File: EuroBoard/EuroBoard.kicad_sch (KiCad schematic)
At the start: 13 parts, among them J1 UART, SW1 SW_SPST, U2 STM32G030CxT, Y1 16MHz

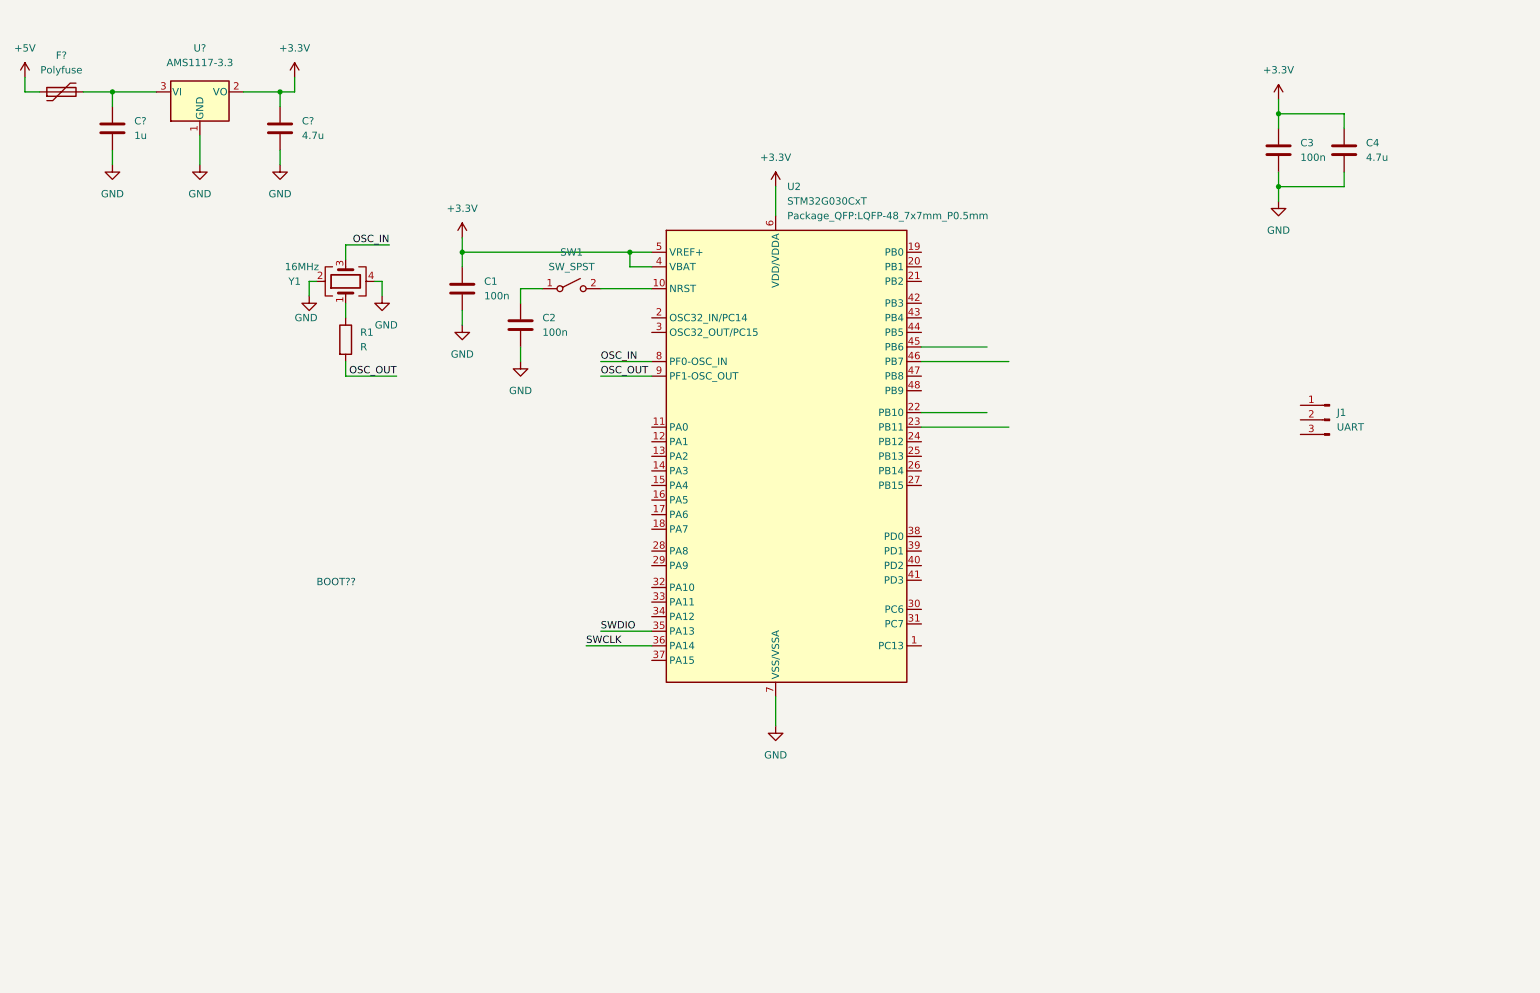
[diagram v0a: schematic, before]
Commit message: EuroBoard connector added
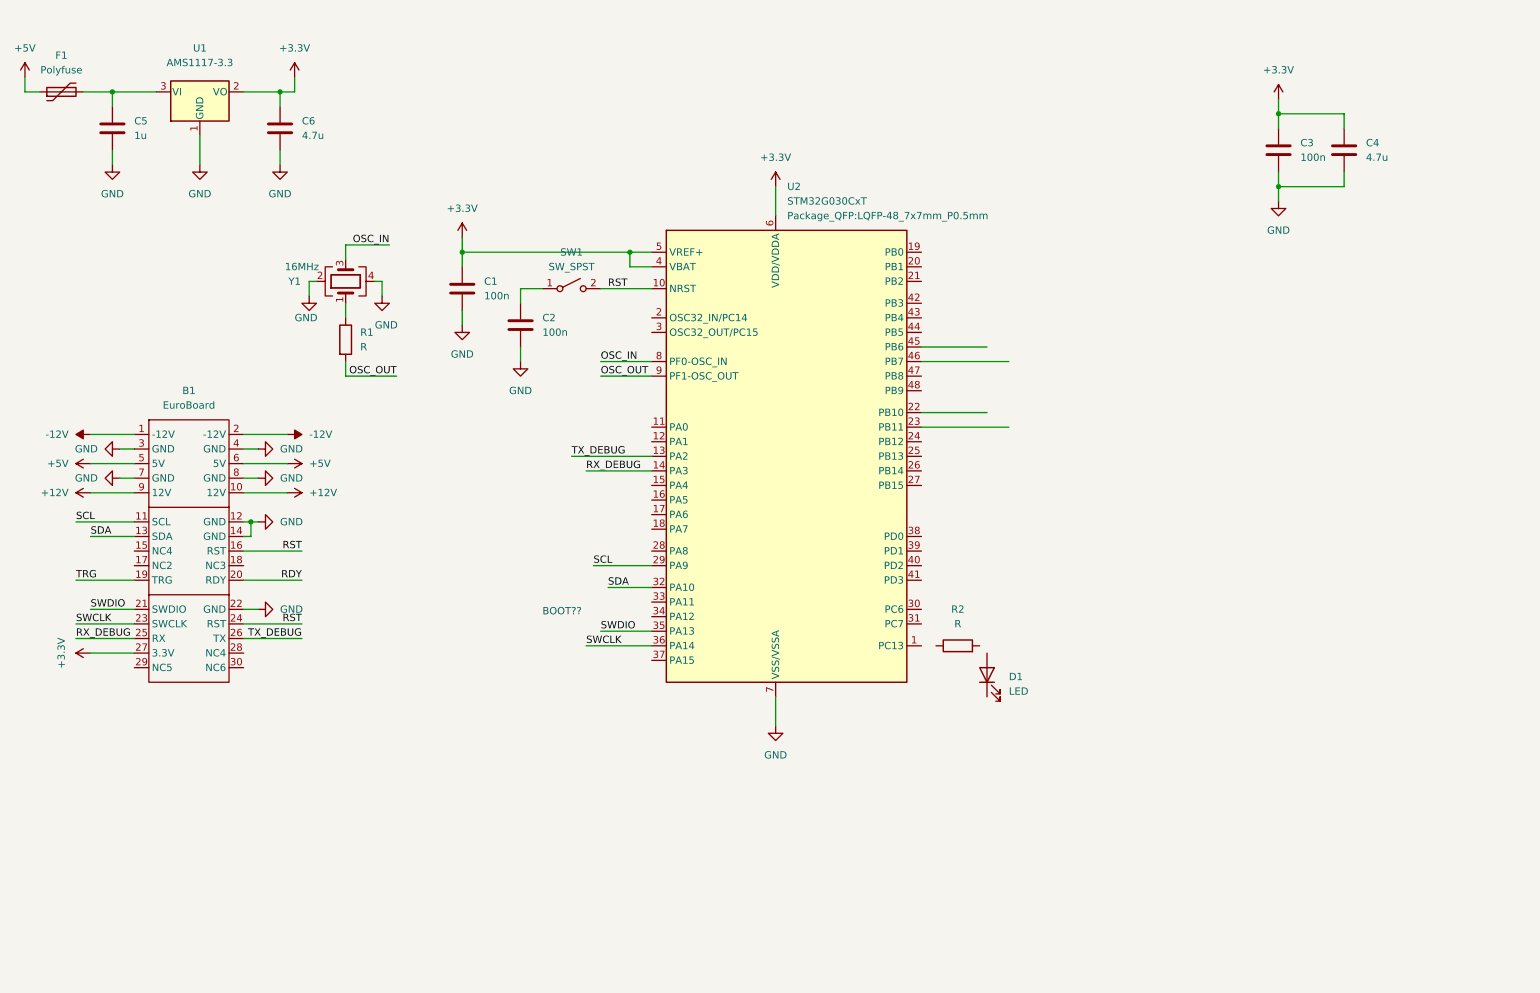
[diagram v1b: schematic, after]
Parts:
- removed J1: UART, symbol Connector:Conn_01x03_Male
- added B1: EuroBoard, MEMS_Custom:EuroMeasure, symbol MEMS_Custom:EuroBoard
- added D1: LED, symbol Device:LED
- added R2: R, Resistor_SMD:R_0805_2012Metric_Pad1.20x1.40mm_HandSolder, symbol Device:R
- C1, C2, C3, C4: footprint (none) -> Capacitor_SMD:C_0805_2012Metric_Pad1.18x1.45mm_HandSolder
- C5, C6: renamed from C?; footprint (none) -> Capacitor_SMD:C_0805_2012Metric_Pad1.18x1.45mm_HandSolder
- R1: footprint (none) -> Resistor_SMD:R_0805_2012Metric_Pad1.20x1.40mm_HandSolder
- Y1: footprint (none) -> Oscillator:Oscillator_SMD_Abracon_ASDMB-4Pin_2.5x2.0mm
- gave numbers to parts that had none: 2
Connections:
- net +3.3V: now also B1.27 (3.3V)
- net +5V: now also B1.5 (5V), B1.6 (5V)
- net GND: now also B1.12 (GND), B1.14 (GND), B1.22 (GND), B1.3 (GND), B1.4 (GND), B1.7 (GND), B1.8 (GND)
- net SWCLK: now also B1.23 (SWCLK)
- net SWDIO: now also B1.21 (SWDIO)
- net RST: now reaches SW1.2 (B), U2.10 (NRST)
- net RST: now also B1.16 (RST), B1.24 (RST)
- net TX_DEBUG: now reaches U2.13 (PA2)
- net TX_DEBUG: now also B1.26 (TX)
- net RX_DEBUG: now reaches U2.14 (PA3)
- net RX_DEBUG: now also B1.25 (RX)
- net SCL: now reaches U2.29 (PA9)
- net SCL: now also B1.11 (SCL)
- net SDA: now reaches U2.32 (PA10)
- net SDA: now also B1.13 (SDA)
- new net +12V: B1.10 (12V), B1.9 (12V)
- new net -12V: B1.1 (-12V), B1.2 (-12V)
- new net RDY: B1.20 (RDY)
- new net TRG: B1.19 (TRG)

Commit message: mend
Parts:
- added R?: R, Resistor_SMD:R_0805_2012Metric_Pad1.20x1.40mm_HandSolder, symbol Device:R
- added SW?: BOOT, Button_Switch_SMD:SW_SPST_B3U-1000P-B, symbol Switch:SW_SPST
- SW1: value SW_SPST -> RESET
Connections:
- net +3.3V: now also SW?.1 (A)
- net GND: now also D1.1 (K)
- net SWCLK: now also R?.1
- net at R2.1: now also D1.2 (A)
- net at R2.2: now also U2.1 (PC13)
- new net: R?.2, SW?.2 (B)
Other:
- moved on the sheet: D1, R2

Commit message: Almost done
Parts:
- removed R?: R, Resistor_SMD:R_0805_2012Metric_Pad1.20x1.40mm_HandSolder, symbol Device:R
- removed SW?: BOOT, Button_Switch_SMD:SW_SPST_B3U-1000P-B, symbol Switch:SW_SPST
- added C7: C, Capacitor_SMD:C_0805_2012Metric_Pad1.18x1.45mm_HandSolder, symbol Device:C
- added C8: 100n, Capacitor_SMD:C_0805_2012Metric_Pad1.18x1.45mm_HandSolder, symbol Device:C
- added D?: 1n4148, Diode_SMD:D_SOD-123, symbol Device:D
- added J1: SPI, Connector_PinHeader_2.54mm:PinHeader_1x04_P2.54mm_Vertical, symbol Connector:Conn_01x04_Male
- added J?: UART, symbol Connector:Conn_01x03_Male
- added J?: I2C, symbol Connector:Conn_01x03_Male
- added L1: L_Ferrite, Inductor_SMD:L_0805_2012Metric, symbol Device:L_Ferrite
- C1: value 100n -> C
- D1: footprint (none) -> LED_SMD:LED_0805_2012Metric_Pad1.15x1.40mm_HandSolder
- F1: footprint (none) -> Fuse:Fuse_1210_3225Metric
- R2: value R -> 1k
- SW1: footprint Button_Switch_SMD:SW_SPST_B3U-1000P-B -> Button_Switch_SMD:SW_SPST_B3S-1000
- Y1: value 16MHz -> NX2520 16MHz
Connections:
- net +3.3V: no longer C1.1, U2.5 (VREF+)
- net GND: now also SW1.1 (A), C7.2, C8.2, J1.4 (Pin_4), J?.3 (Pin_3), J?.3 (Pin_3)
- net OSC_IN: now also C1.1
- net RST: now also D?.1 (K); no longer SW1.2 (B), U2.10 (NRST)
- net SCL: now also U2.45 (PB6); no longer U2.29 (PA9)
- net SDA: now also U2.46 (PB7); no longer U2.32 (PA10)
- net at C5.1, U1.3 (VI): now also L1.2; no longer F1.2
- net at C2.1: now also SW1.2 (B), U2.10 (NRST), D?.2 (A); no longer SW1.1 (A)
- net LED: now reaches R2.2, U2.1 (PC13)
- net SPI1_SCK: now reaches U2.12 (PA1)
- net SPI1_SCK: now also J1.1 (Pin_1)
- net SPI1_MISO: now reaches U2.17 (PA6)
- net SPI1_MISO: now also J1.2 (Pin_2), J1.3 (Pin_3)
- net SPI1_MOSI: now reaches U2.18 (PA7)
- net SCL2: now reaches U2.22 (PB10)
- net SCL2: now also J?.1 (Pin_1)
- net SDA2: now reaches U2.23 (PB11)
- net SDA2: now also J?.2 (Pin_2)
- net at R1.1, Y1.1: now also C7.1
- new net: F1.2, L1.1
- new net RX_AUX: J?.2 (Pin_2), U2.32 (PA10)
- new net TX_AUX: J?.1 (Pin_1), U2.29 (PA9)
- new net VREF: C8.1, U2.5 (VREF+)
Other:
- note added: "BOOT0"
- note removed: "BOOT??"
- moved on the sheet: B1, C2, C3, C4, C5, C6, D1, F1, R1, R2, SW1, U1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

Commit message: Almost done
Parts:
- gave numbers to parts that had none: 3
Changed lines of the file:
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@@
   (symbol (lib_id "Connector:Conn_01x03_Male") (at 241.3 109.22 0) (unit 1)
     (in_bom yes) (on_board yes) (fields_autoplaced)
-    (property "Reference" "J?" (id 0) (at 241.935 101.6 0))
+    (property "Reference" "J3" (id 0) (at 241.935 101.6 0))
     (property "Value" "UART" (id 1) (at 241.935 104.14 0))
     (property "Footprint" "" (id 2) (at 241.3 109.22 0)
@@
   (symbol (lib_id "power:GND") (at 248.92 111.76 0) (unit 1)
     (in_bom yes) (on_board yes) (fields_autoplaced)
-    (property "Reference" "#PWR?" (id 0) (at 248.92 118.11 0)
+    (property "Reference" "#PWR0105" (id 0) (at 248.92 118.11 0)
       (effects (font (size 1.27 1.27)) hide)
     )
@@
   (symbol (lib_id "Connector:Conn_01x03_Male") (at 241.3 91.44 0) (unit 1)
     (in_bom yes) (on_board yes) (fields_autoplaced)
-    (property "Reference" "J?" (id 0) (at 241.935 83.82 0))
+    (property "Reference" "J2" (id 0) (at 241.935 83.82 0))
     (property "Value" "I2C" (id 1) (at 241.935 86.36 0))
     (property "Footprint" "" (id 2) (at 241.3 91.44 0)
@@
   (symbol (lib_id "Device:D") (at 97.79 64.77 0) (unit 1)
     (in_bom yes) (on_board yes) (fields_autoplaced)
-    (property "Reference" "D?" (id 0) (at 97.79 58.42 0))
+    (property "Reference" "D2" (id 0) (at 97.79 58.42 0))
     (property "Value" "1n4148" (id 1) (at 97.79 60.96 0))
     (property "Footprint" "Diode_SMD:D_SOD-123" (id 2) (at 97.79 64.77 0)
@@
   (symbol (lib_id "power:GND") (at 248.92 93.98 0) (unit 1)
     (in_bom yes) (on_board yes) (fields_autoplaced)
-    (property "Reference" "#PWR?" (id 0) (at 248.92 100.33 0)
+    (property "Reference" "#PWR0128" (id 0) (at 248.92 100.33 0)
       (effects (font (size 1.27 1.27)) hide)
     )
@@
   (symbol (lib_id "power:GND") (at 250.19 41.91 0) (unit 1)
     (in_bom yes) (on_board yes) (fields_autoplaced)
-    (property "Reference" "#PWR?" (id 0) (at 250.19 48.26 0)
+    (property "Reference" "#PWR0129" (id 0) (at 250.19 48.26 0)
       (effects (font (size 1.27 1.27)) hide)
     )
@@
       (reference "#PWR0104") (unit 1) (value "GND") (footprint "")
     )
+    (path "/7d243bd9-5a2e-4326-8d2b-a5f1dfd1f8f3"
+      (reference "#PWR0105") (unit 1) (value "GND") (footprint "")
+    )
     (path "/302a3ca2-8721-479b-b4eb-f005cb527499"
       (reference "#PWR0106") (unit 1) (value "GND") (footprint "")
@@
       (reference "#PWR0127") (unit 1) (value "GND") (footprint "")
     )
-    (path "/7d243bd9-5a2e-4326-8d2b-a5f1dfd1f8f3"
-      (reference "#PWR?") (unit 1) (value "GND") (footprint "")
-    )
     (path "/c7143079-c7d7-419c-9261-2f446fb4d84f"
-      (reference "#PWR?") (unit 1) (value "GND") (footprint "")
+      (reference "#PWR0128") (unit 1) (value "GND") (footprint "")
     )
     (path "/e1d04403-db45-42b9-aeee-a12acba02ccf"
-      (reference "#PWR?") (unit 1) (value "GND") (footprint "")
+      (reference "#PWR0129") (unit 1) (value "GND") (footprint "")
     )
     (path "/d92283e0-1a84-4854-b416-29c1c54c41f7"
@@
     )
     (path "/acef170c-9dde-4b25-b979-ff4ef70a5cbb"
-      (reference "D?") (unit 1) (value "1n4148") (footprint "Diode_SMD:D_SOD-123")
+      (reference "D2") (unit 1) (value "1n4148") (footprint "Diode_SMD:D_SOD-123")
     )
     (path "/55ad175e-3839-4c69-a4d0-462ebdbf17e1"
@@
       (reference "J1") (unit 1) (value "SPI") (footprint "Connector_PinHeader_2.54mm:PinHeader_1x04_P2.54mm_Vertical")
     )
+    (path "/a131e4fd-2b6b-4ceb-827a-fe46605e4cbb"
+      (reference "J2") (unit 1) (value "I2C") (footprint "")
+    )
     (path "/2486761d-6715-4e29-a9bb-d5aae2207d95"
-      (reference "J?") (unit 1) (value "UART") (footprint "")
-    )
-    (path "/a131e4fd-2b6b-4ceb-827a-fe46605e4cbb"
-      (reference "J?") (unit 1) (value "I2C") (footprint "")
+      (reference "J3") (unit 1) (value "UART") (footprint "")
     )
     (path "/c2e8100f-910e-434c-951c-160188608971"

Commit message: Started doing PCB
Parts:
- added C10: 100n, Capacitor_SMD:C_0805_2012Metric_Pad1.18x1.45mm_HandSolder, symbol Device:C
- added C11, C9: 10u, Capacitor_SMD:C_0805_2012Metric_Pad1.18x1.45mm_HandSolder, symbol Device:C
- C4: value 4.7u -> 10u
- J2, J3: footprint (none) -> Connector_PinSocket_2.54mm:PinSocket_1x03_P2.54mm_Vertical
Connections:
- net +3.3V: now also L1.2, C10.1, C11.1; no longer C6.1, U1.2 (VO)
- net GND: now also C10.2, C11.2, C9.2
- net at C5.1, U1.3 (VI): now also F1.2, C9.1; no longer L1.2
- net at L1.1: now also C6.1, U1.2 (VO); no longer F1.2
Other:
- moved on the sheet: C5, C6, F1, L1, U1

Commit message: Board outline
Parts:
- removed J1: SPI, Connector_PinHeader_2.54mm:PinHeader_1x04_P2.54mm_Vertical, symbol Connector:Conn_01x04_Male
- removed J2: I2C, Connector_PinSocket_2.54mm:PinSocket_1x03_P2.54mm_Vertical, symbol Connector:Conn_01x03_Male
- added C12, C13, C14, C15: 10u, Capacitor_SMD:C_0805_2012Metric_Pad1.18x1.45mm_HandSolder, symbol Device:C
- added J1: GPIO, Connector_PinHeader_2.54mm:PinHeader_1x08_P2.54mm_Vertical, symbol Connector:Conn_01x08_Male
- added J2: Conn_01x07_Male, Connector_PinHeader_2.54mm:PinHeader_1x07_P2.54mm_Vertical, symbol Connector:Conn_01x07_Male
- added J4: Conn_01x05_Male, Connector_PinHeader_2.54mm:PinHeader_1x05_P2.54mm_Vertical, symbol Connector:Conn_01x05_Male
- added SW2: SW_DIP_x04, Button_Switch_SMD:SW_DIP_SPSTx04_Slide_Omron_A6H-4101_W6.15mm_P1.27mm, symbol Switch:SW_DIP_x04
- C4: value 10u -> 4.7u
- J3: value UART -> I2C; footprint Connector_PinSocket_2.54mm:PinSocket_1x03_P2.54mm_Vertical -> Connector_PinHeader_2.54mm:PinHeader_1x03_P2.54mm_Vertical
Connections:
- net +12V: now also C15.1, J4.4 (Pin_4)
- net +3.3V: now also C12.1, J4.1 (Pin_1)
- net +5V: now also C14.1, J4.3 (Pin_3)
- net -12V: now also C13.1, J4.2 (Pin_2)
- net GND: now also C12.2, C13.2, C14.2, C15.2, J4.5 (Pin_5), SW2.5, SW2.6, SW2.7, SW2.8
- net RDY: now also U2.20 (PB1)
- net RX_AUX: no longer J3.2 (Pin_2)
- net RX_DEBUG: now also J1.4 (Pin_4)
- net SCL: now also J2.4 (Pin_4)
- net SCL2: now also J3.1 (Pin_1)
- net SDA: now also J2.5 (Pin_5)
- net SDA2: now also J3.2 (Pin_2)
- net SPI1_MISO: now also J1.7 (Pin_7)
- net SPI1_MOSI: now also J1.8 (Pin_8)
- net SPI1_SCK: now also J1.2 (Pin_2)
- net TRG: now also U2.19 (PB0)
- net TX_AUX: no longer J3.1 (Pin_1)
- net TX_DEBUG: now also J1.3 (Pin_3)
- net at U2.11 (PA0): now also J1.1 (Pin_1)
- net at U2.15 (PA4): now also J1.5 (Pin_5)
- net at U2.16 (PA5): now also J1.6 (Pin_6)
- net at U2.24 (PB12): now also SW2.4
- net at U2.25 (PB13): now also SW2.3
- net at U2.26 (PB14): now also SW2.2
- net at U2.27 (PB15): now also SW2.1
- net at U2.42 (PB3): now also J2.1 (Pin_1)
- net at U2.43 (PB4): now also J2.2 (Pin_2)
- net at U2.44 (PB5): now also J2.3 (Pin_3)
- net at U2.47 (PB8): now also J2.6 (Pin_6)
- net at U2.48 (PB9): now also J2.7 (Pin_7)

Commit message: Board awaiting review
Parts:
- removed C10, C3: 100n, Capacitor_SMD:C_0805_2012Metric_Pad1.18x1.45mm_HandSolder, symbol Device:C
- added J10: PD1, TestPoint:TestPoint_Pad_1.0x1.0mm, symbol Connector:Conn_01x01_Male
- added J11: PD2, TestPoint:TestPoint_Pad_1.0x1.0mm, symbol Connector:Conn_01x01_Male
- added J12: PD3, TestPoint:TestPoint_Pad_1.0x1.0mm, symbol Connector:Conn_01x01_Male
- added J5: RX, TestPoint:TestPoint_Pad_1.0x1.0mm, symbol Connector:Conn_01x01_Male
- added J6: TX, TestPoint:TestPoint_Pad_1.0x1.0mm, symbol Connector:Conn_01x01_Male
- added J7: GND, TestPoint:TestPoint_Pad_1.0x1.0mm, symbol Connector:Conn_01x01_Male
- L1: footprint Inductor_SMD:L_0805_2012Metric -> Inductor_SMD:L_0805_2012Metric_Pad1.15x1.40mm_HandSolder
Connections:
- net GND: now also J7.1 (Pin_1)
- net RX_AUX: now also J5.1 (Pin_1)
- net TX_AUX: now also J6.1 (Pin_1)
- net at U2.39 (PD1): now also J10.1 (Pin_1)
- net at U2.40 (PD2): now also J11.1 (Pin_1)
- net at U2.41 (PD3): now also J12.1 (Pin_1)
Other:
- moved on the sheet: C4
